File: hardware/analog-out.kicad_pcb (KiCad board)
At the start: 2 copper layers, 30 x 35 mm, 29 parts, among them P1 CON-SENSOR, P2 CONN_5, U1 M24C64, U2 MCP4725A0, U3 TLV272IS, U4 DRILL, U5 DRILL, U6 DRILL, U7 DRILL

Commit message: order version
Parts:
- moved Ref** 0.68 mm to (153.3, 112.0)

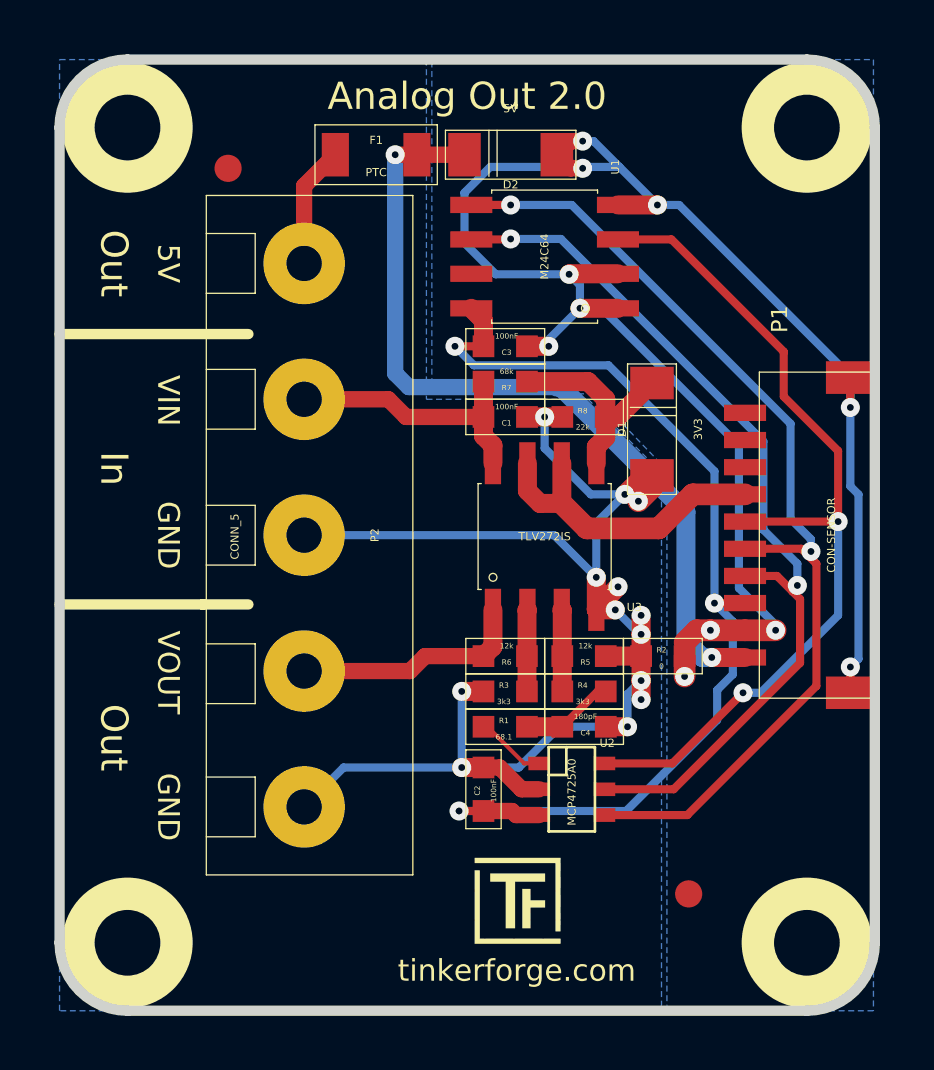
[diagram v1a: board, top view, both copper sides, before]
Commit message: change port description
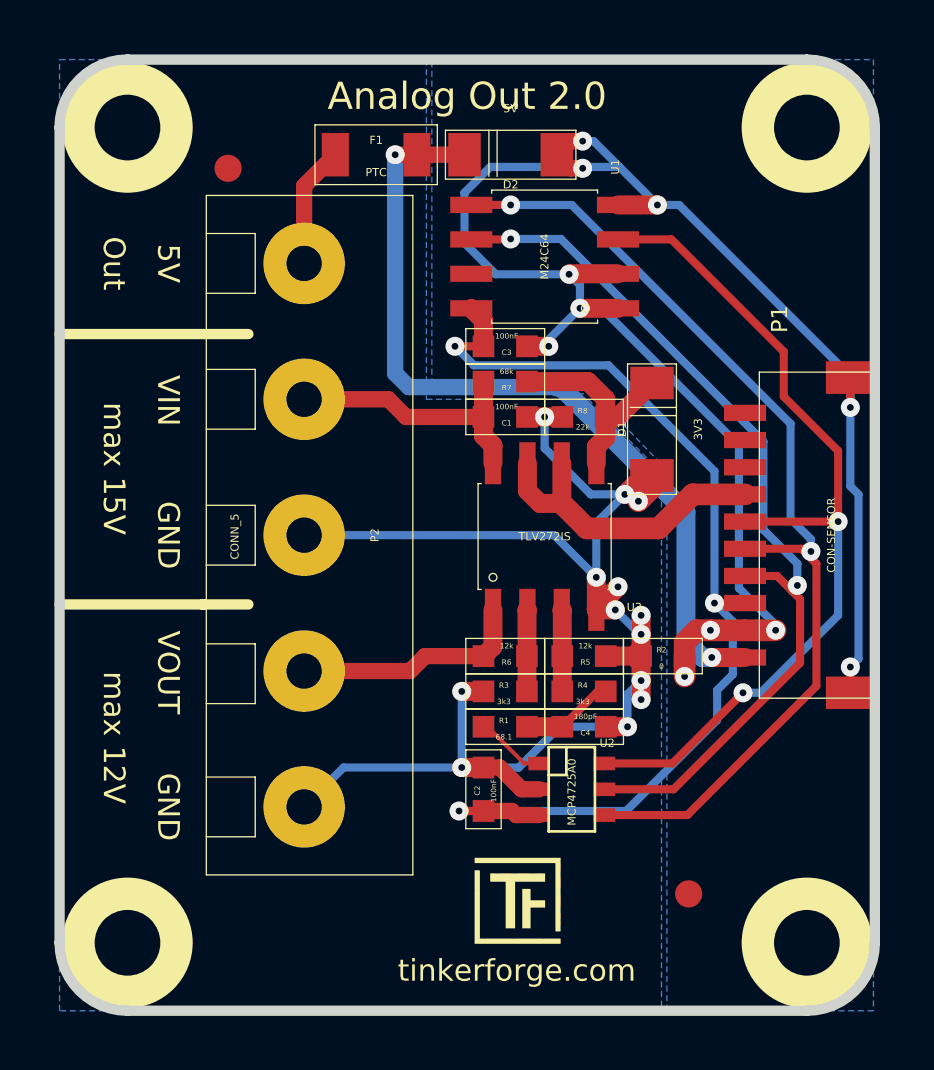
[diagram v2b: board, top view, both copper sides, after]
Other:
- board text added: "max 12V"
- board text added: "max 15V"
- board text removed: "In"

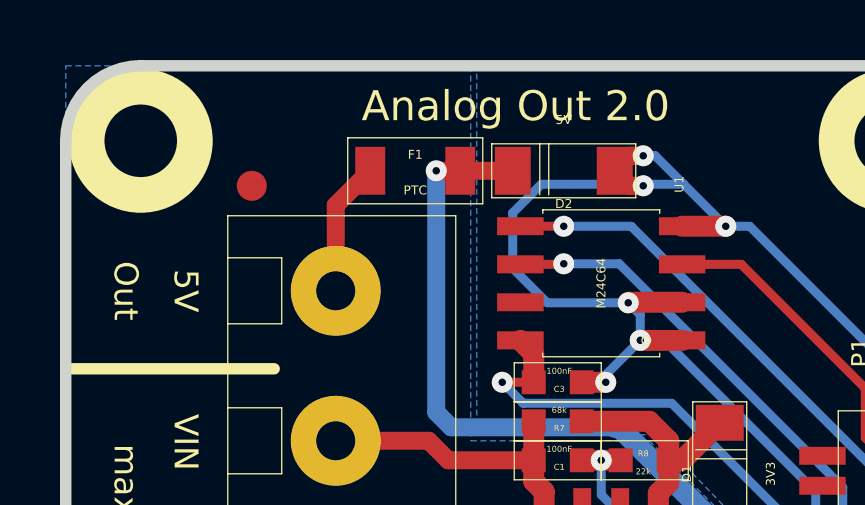
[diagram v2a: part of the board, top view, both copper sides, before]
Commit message: specify fuse
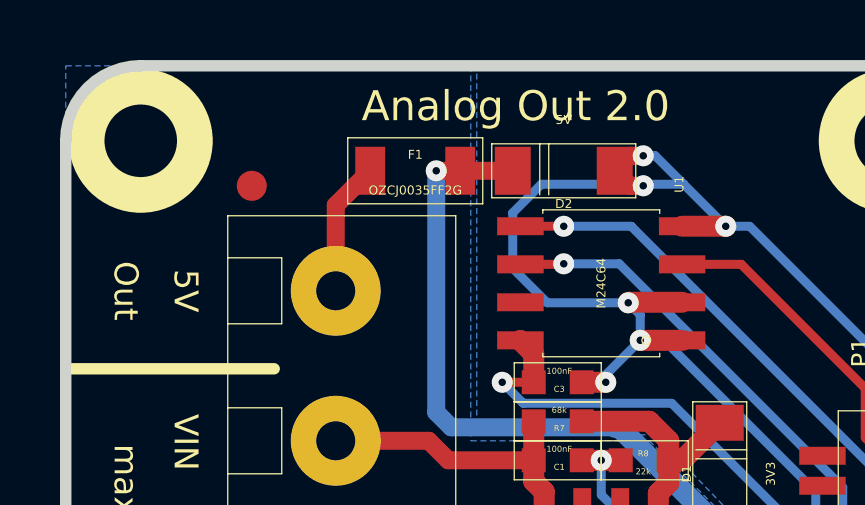
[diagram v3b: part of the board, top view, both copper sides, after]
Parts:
- F1: value PTC -> OZCJ0035FF2G

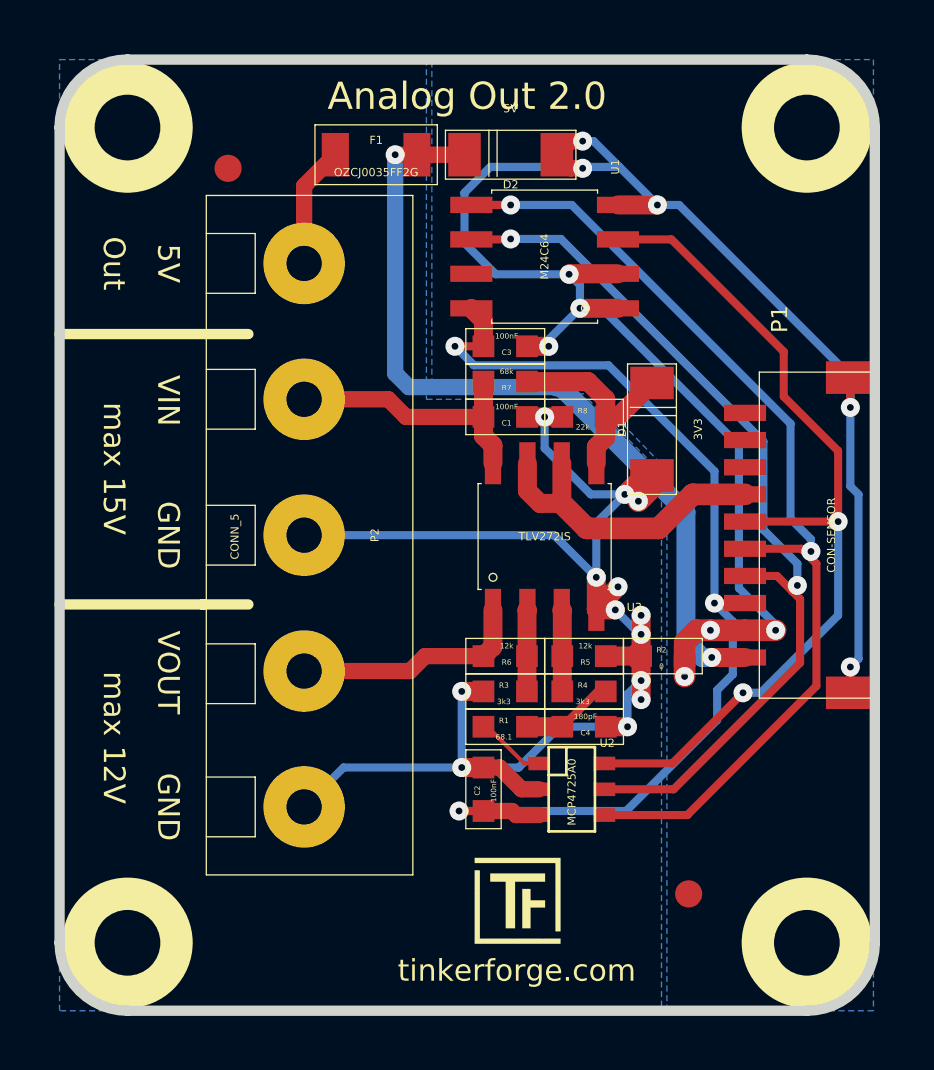
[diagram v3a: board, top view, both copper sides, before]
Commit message: change voltage devider to opamp differential amplifier
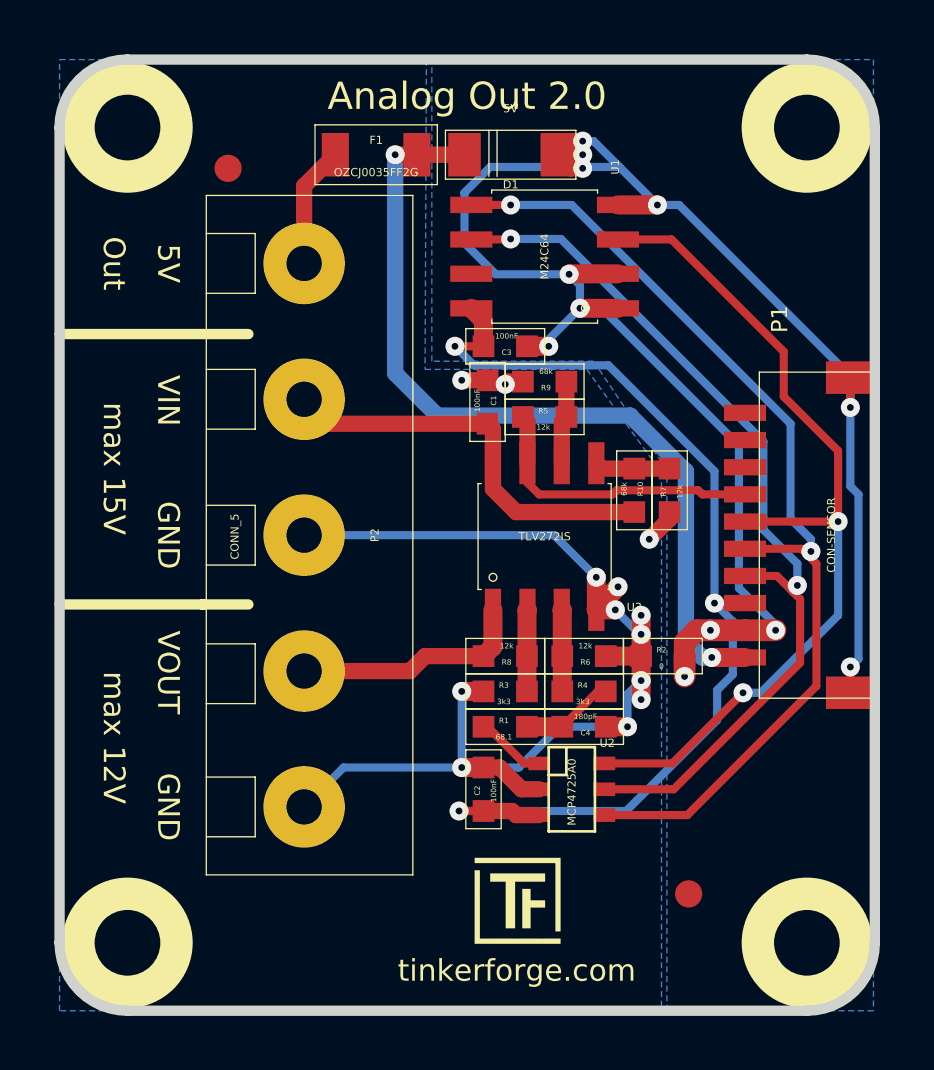
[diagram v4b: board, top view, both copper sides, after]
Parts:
- removed D2: 5V, kicad-libraries:MiniMelf
- added R10: 68k, kicad-libraries:0603, F.Cu at (159.2, 98.4)
- added R9: 68k, kicad-libraries:0603, F.Cu at (155.9, 94.4)
- D1: value 3V3 -> 5V
- R7: value 68k -> 12k
- R8: value 22k -> 12k
- moved D1 11.4 mm to (154.7, 86.1), turned to 0 degrees
- moved R8 9.27 mm to (154.4, 104.5), turned to 0 degrees
- moved R5 8.92 mm to (155.9, 95.7), turned to 180 degrees
- moved R7 7.25 mm to (160.5, 98.4), turned to 270 degrees
- moved R6 2.90 mm to (157.3, 104.5)
- moved C1 0.85 mm to (153.8, 95.2), turned to 90 degrees
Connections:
- D1 pad 1: AGND -> GND
- D1 pad 2: Net-(D1-Pad2) -> +5V
- R5 pad 1: Net-(R4-Pad2) -> Net-(R5-Pad1)
- R5 pad 2: AGND -> Net-(P1-Pad7)
- R6 pad 1: Net-(P2-Pad2) -> Net-(R4-Pad2)
- R6 pad 2: Net-(R3-Pad1) -> AGND
- R7 pad 1: VCC -> Net-(R10-Pad2)
- R7 pad 2: Net-(D1-Pad2) -> AGND
- R8 pad 1: Net-(D1-Pad2) -> Net-(P2-Pad2)
- R8 pad 2: AGND -> Net-(R3-Pad1)
- U3 pad 5: Net-(D1-Pad2) -> Net-(R10-Pad2)
- U3 pad 6: Net-(P1-Pad7) -> Net-(R5-Pad1)
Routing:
- net AGND: track 54.8 -> 45.8 mm
- net Net-(D1-Pad2): track 7.88 -> 0.00 mm
- net VCC: track 10.0 -> 15.2 mm
- net Net-(R5-Pad1): track 0.00 -> 3.07 mm
- net Net-(R10-Pad2): track 0.00 -> 2.78 mm
- net GND: track 69.9 -> 70.9 mm, vias 11 -> 12
- net +5V: track 30.6 -> 31.5 mm
- net Net-(P1-Pad7): track 11.6 -> 10.8 mm
